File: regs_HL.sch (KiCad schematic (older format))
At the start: 32 parts, among them U30 74HC373, U31 74HC373, U32 74HC244, U33 74HC244, U34 74HC244, U35 74HC244

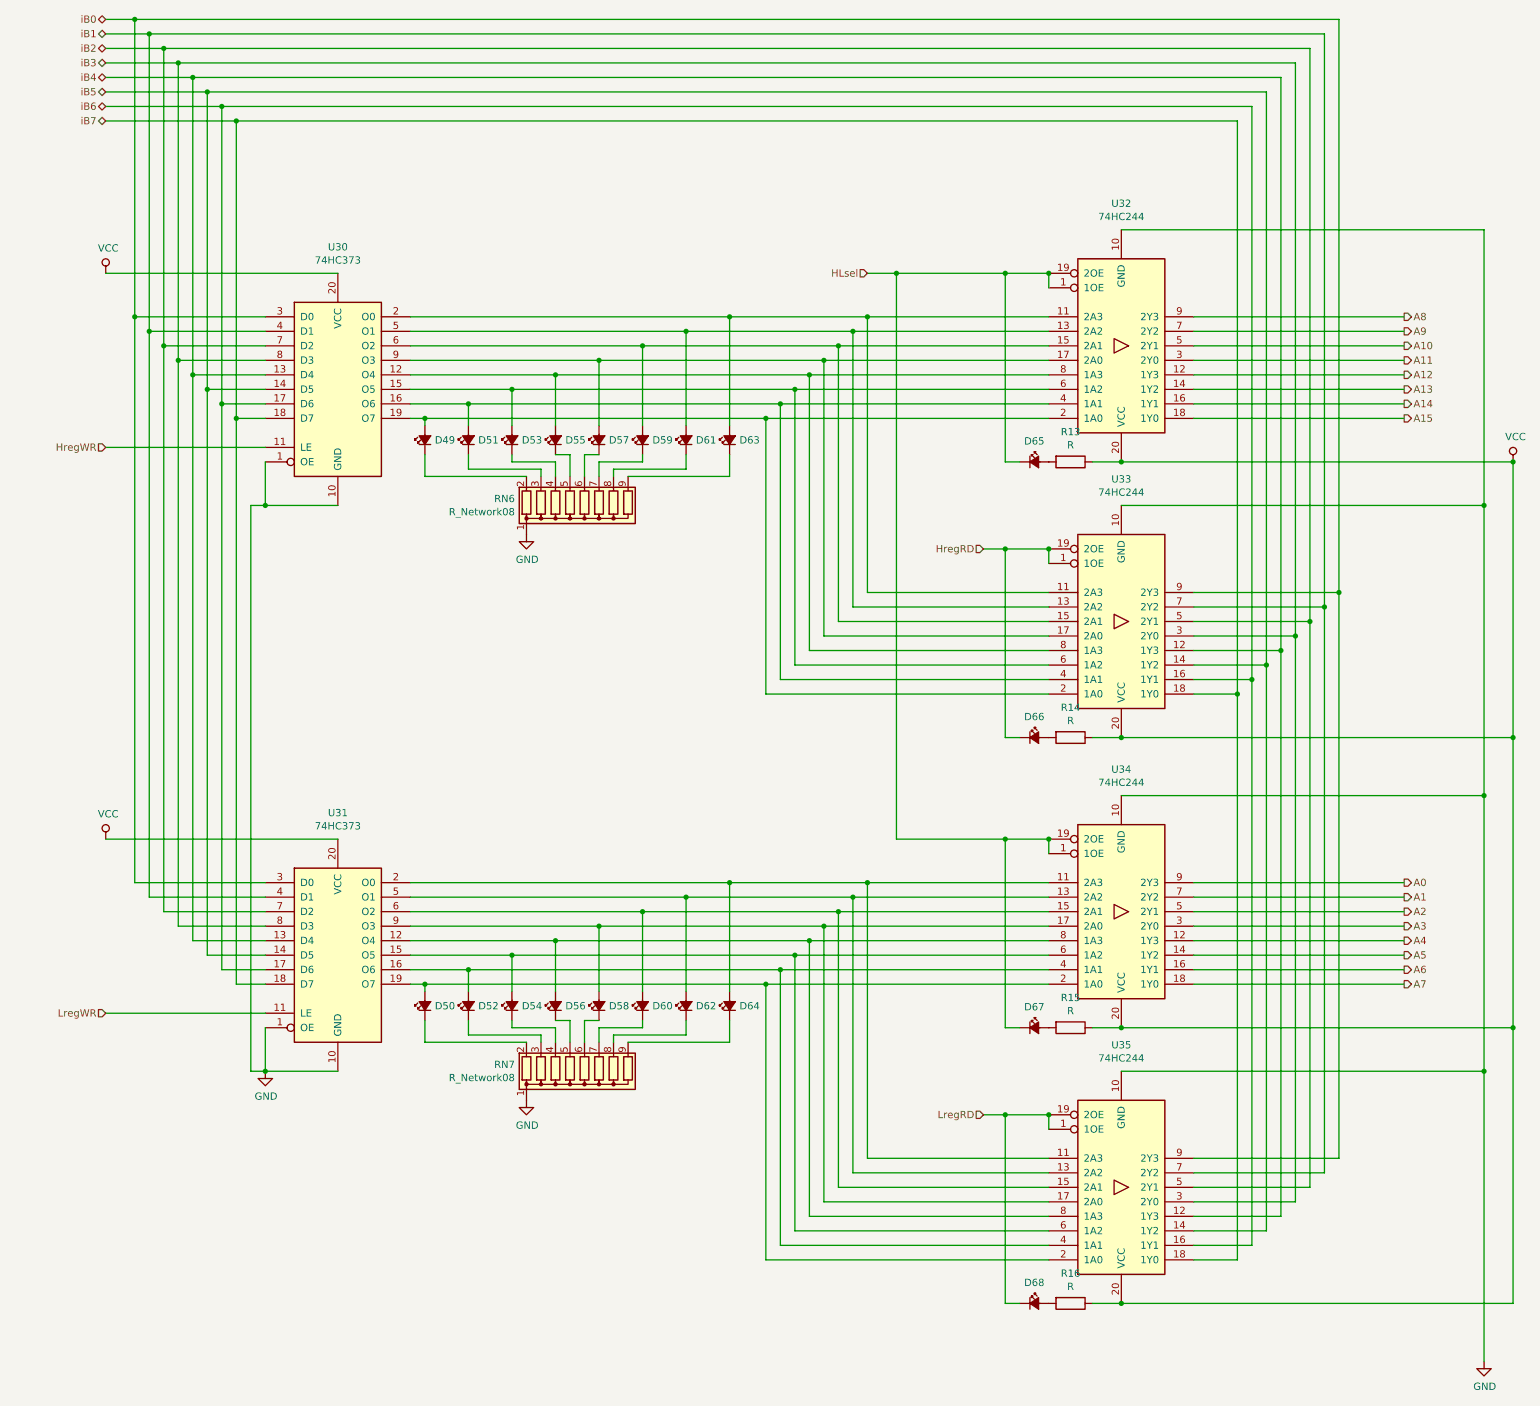
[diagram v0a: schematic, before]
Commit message: annotate HL registers
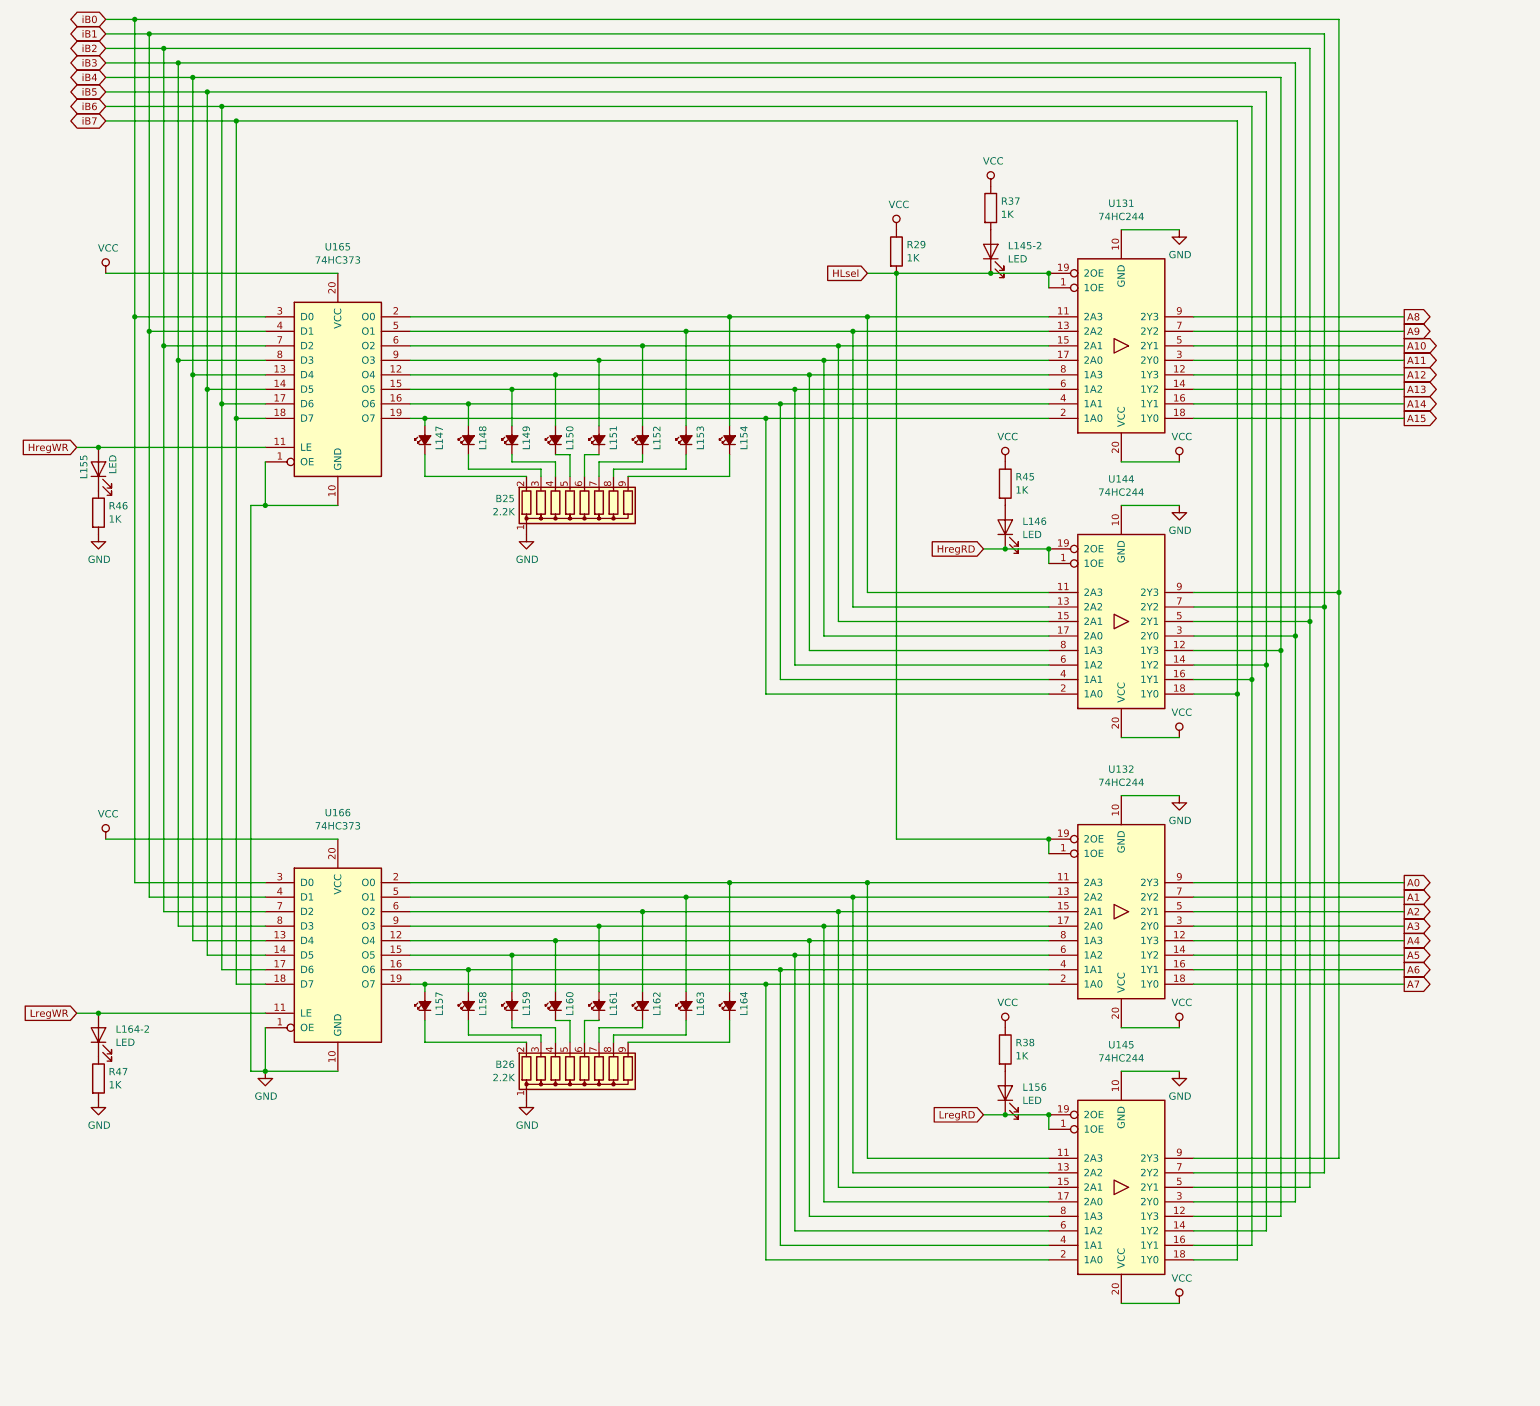
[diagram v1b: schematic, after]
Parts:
- removed D65, D66, D67, D68: LED_Small_ALT, LED_THT:LED_D3.0mm, symbol Device:LED_Small_ALT
- removed R13, R14, R15, R16: R, Resistor_THT:R_Axial_DIN0207_L6.3mm_D2.5mm_P10.16mm_Horizontal, symbol Device:R
- added L145-2, L146, L155, L156, L164-2: LED, symbol Device:LED
- added R29, R37, R38, R45, R46, R47: 1K, symbol Device:R
- B25: renamed from RN6; value R_Network08 -> 2.2K
- B26: renamed from RN7; value R_Network08 -> 2.2K
- renumbered D49 to L147, D51 to L148, D53 to L149, D55 to L150, D57 to L151, D59 to L152, D61 to L153, D63 to L154, D50 to L157, D52 to L158, D54 to L159, D56 to L160, D58 to L161, D60 to L162, D62 to L163, D64 to L164, U32 to U131, U34 to U132, U33 to U144, U35 to U145, U30 to U165, U31 to U166
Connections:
- net GND: now also R46.2, R47.2
- net HLsel: now also L145-2.1 (K), R29.2
- net HregRD: now also L146.1 (K)
- net HregWR: now also L155.2 (A)
- net LregRD: now also L156.1 (K)
- net LregWR: now also L164-2.2 (A)
- net VCC: now also R29.1, R37.1, R38.1, R45.1
- new net: L156.2 (A), R38.2
- new net: L164-2.1 (K), R47.1
- new net: L146.2 (A), R45.2
- new net: L145-2.2 (A), R37.2
- new net: L155.1 (K), R46.1

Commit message: route A8-A15 to U131
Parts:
- L145-2, L146, L155, L156, L164-2: footprint (none) -> LED_THT:LED_D3.0mm
- R29, R37, R38, R45, R46, R47: footprint (none) -> Resistor_THT:R_Axial_DIN0204_L3.6mm_D1.6mm_P5.08mm_Horizontal
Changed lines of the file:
@@
 F 0 "L156" V 7289 8082 50  0000 R CNN
 F 1 "LED" V 7198 8082 50  0000 R CNN
-F 2 "" H 7250 8200 50  0001 C CNN
+F 2 "LED_THT:LED_D3.0mm" H 7250 8200 50  0001 C CNN
 F 3 "~" H 7250 8200 50  0001 C CNN
 	1    7250 8200
@@
 F 0 "R38" H 7320 7946 50  0000 L CNN
 F 1 "1K" H 7320 7855 50  0000 L CNN
-F 2 "" V 7180 7900 50  0001 C CNN
+F 2 "Resistor_THT:R_Axial_DIN0204_L3.6mm_D1.6mm_P5.08mm_Horizontal" V 7180 7900 50  0001 C CNN
 F 3 "~" H 7250 7900 50  0001 C CNN
 	1    7250 7900
@@
 F 0 "L164-2" V 1039 7682 50  0000 R CNN
 F 1 "LED" V 948 7682 50  0000 R CNN
-F 2 "" H 1000 7800 50  0001 C CNN
+F 2 "LED_THT:LED_D3.0mm" H 1000 7800 50  0001 C CNN
 F 3 "~" H 1000 7800 50  0001 C CNN
 	1    1000 7800
@@
 F 0 "R47" H 1070 8146 50  0000 L CNN
 F 1 "1K" H 1070 8055 50  0000 L CNN
-F 2 "" V 930 8100 50  0001 C CNN
+F 2 "Resistor_THT:R_Axial_DIN0204_L3.6mm_D1.6mm_P5.08mm_Horizontal" V 930 8100 50  0001 C CNN
 F 3 "~" H 1000 8100 50  0001 C CNN
 	1    1000 8100
@@
 F 0 "L146" V 7289 4182 50  0000 R CNN
 F 1 "LED" V 7198 4182 50  0000 R CNN
-F 2 "" H 7250 4300 50  0001 C CNN
+F 2 "LED_THT:LED_D3.0mm" H 7250 4300 50  0001 C CNN
 F 3 "~" H 7250 4300 50  0001 C CNN
 	1    7250 4300
@@
 F 0 "R45" H 7320 4046 50  0000 L CNN
 F 1 "1K" H 7320 3955 50  0000 L CNN
-F 2 "" V 7180 4000 50  0001 C CNN
+F 2 "Resistor_THT:R_Axial_DIN0204_L3.6mm_D1.6mm_P5.08mm_Horizontal" V 7180 4000 50  0001 C CNN
 F 3 "~" H 7250 4000 50  0001 C CNN
 	1    7250 4000
@@
 F 0 "L145-2" V 7189 2282 50  0000 R CNN
 F 1 "LED" V 7098 2282 50  0000 R CNN
-F 2 "" H 7150 2400 50  0001 C CNN
+F 2 "LED_THT:LED_D3.0mm" H 7150 2400 50  0001 C CNN
 F 3 "~" H 7150 2400 50  0001 C CNN
 	1    7150 2400
@@
 F 0 "R37" H 7220 2146 50  0000 L CNN
 F 1 "1K" H 7220 2055 50  0000 L CNN
-F 2 "" V 7080 2100 50  0001 C CNN
+F 2 "Resistor_THT:R_Axial_DIN0204_L3.6mm_D1.6mm_P5.08mm_Horizontal" V 7080 2100 50  0001 C CNN
 F 3 "~" H 7150 2100 50  0001 C CNN
 	1    7150 2100
@@
 F 0 "R29" H 6570 2446 50  0000 L CNN
 F 1 "1K" H 6570 2355 50  0000 L CNN
-F 2 "" V 6430 2400 50  0001 C CNN
+F 2 "Resistor_THT:R_Axial_DIN0204_L3.6mm_D1.6mm_P5.08mm_Horizontal" V 6430 2400 50  0001 C CNN
 F 3 "~" H 6500 2400 50  0001 C CNN
 	1    6500 2400
@@
 F 0 "L155" H 1100 4000 50  0000 R CNN
 F 1 "LED" H 1100 3800 50  0000 R CNN
-F 2 "" H 1000 3900 50  0001 C CNN
+F 2 "LED_THT:LED_D3.0mm" H 1000 3900 50  0001 C CNN
 F 3 "~" H 1000 3900 50  0001 C CNN
 	1    1000 3900
@@
 F 0 "R46" H 1070 4246 50  0000 L CNN
 F 1 "1K" H 1070 4155 50  0000 L CNN
-F 2 "" V 930 4200 50  0001 C CNN
+F 2 "Resistor_THT:R_Axial_DIN0204_L3.6mm_D1.6mm_P5.08mm_Horizontal" V 930 4200 50  0001 C CNN
 F 3 "~" H 1000 4200 50  0001 C CNN
 	1    1000 4200
